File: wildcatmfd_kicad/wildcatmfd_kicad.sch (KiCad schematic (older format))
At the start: 21 parts, among them SW1 SW_Push, SW10 SW_Push, SW11 SW_Push, SW12 SW_Push, SW13 SW_Push, SW14 SW_Push, SW15 SW_Push, SW16 SW_Push, SW17 SW_Push, SW18 SW_Push, SW19 SW_Push, SW2 SW_Push, SW20 SW_Push, SW3 SW_Push, SW4 SW_Push, SW5 SW_Push, SW6 SW_Push, SW7 SW_Push, SW8 SW_Push, SW9 SW_Push, U1 Teensy3.6

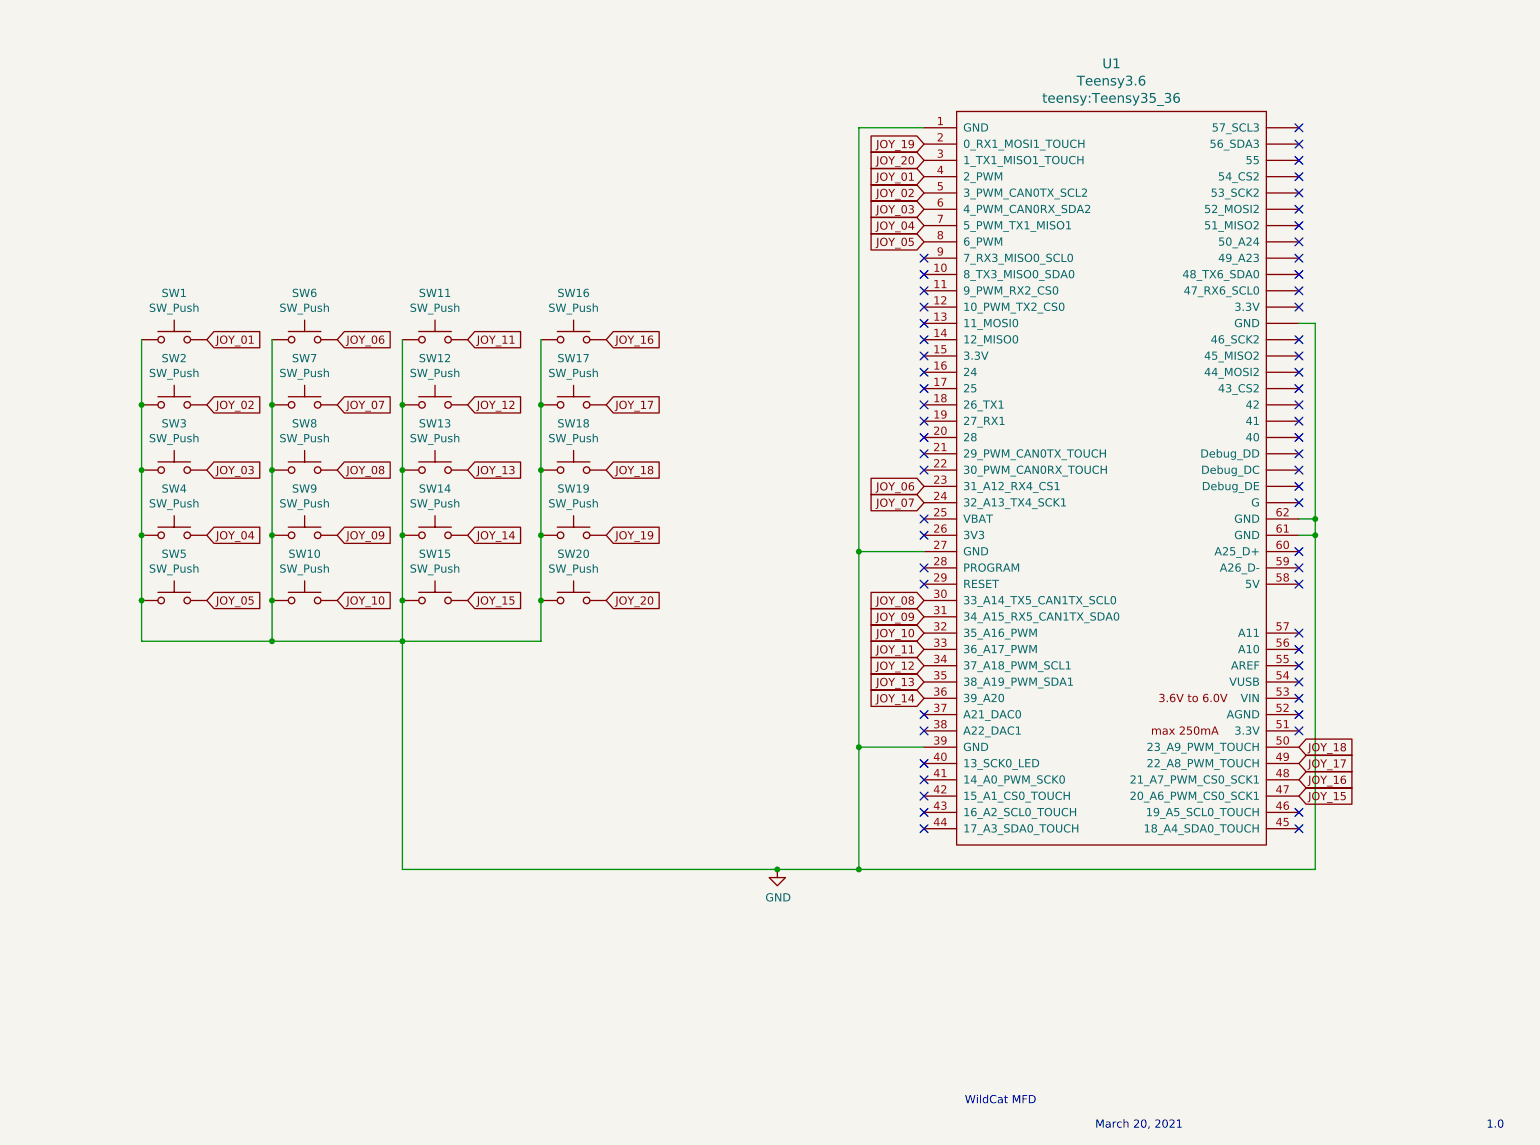
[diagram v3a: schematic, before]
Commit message: PCB 2.0
First attempt - 20mm off on screen mount (doh!) - Redesigning PCB to include pass-thru hole for HDMI ribbon cable and adding 3 pin header for +5v for screen power
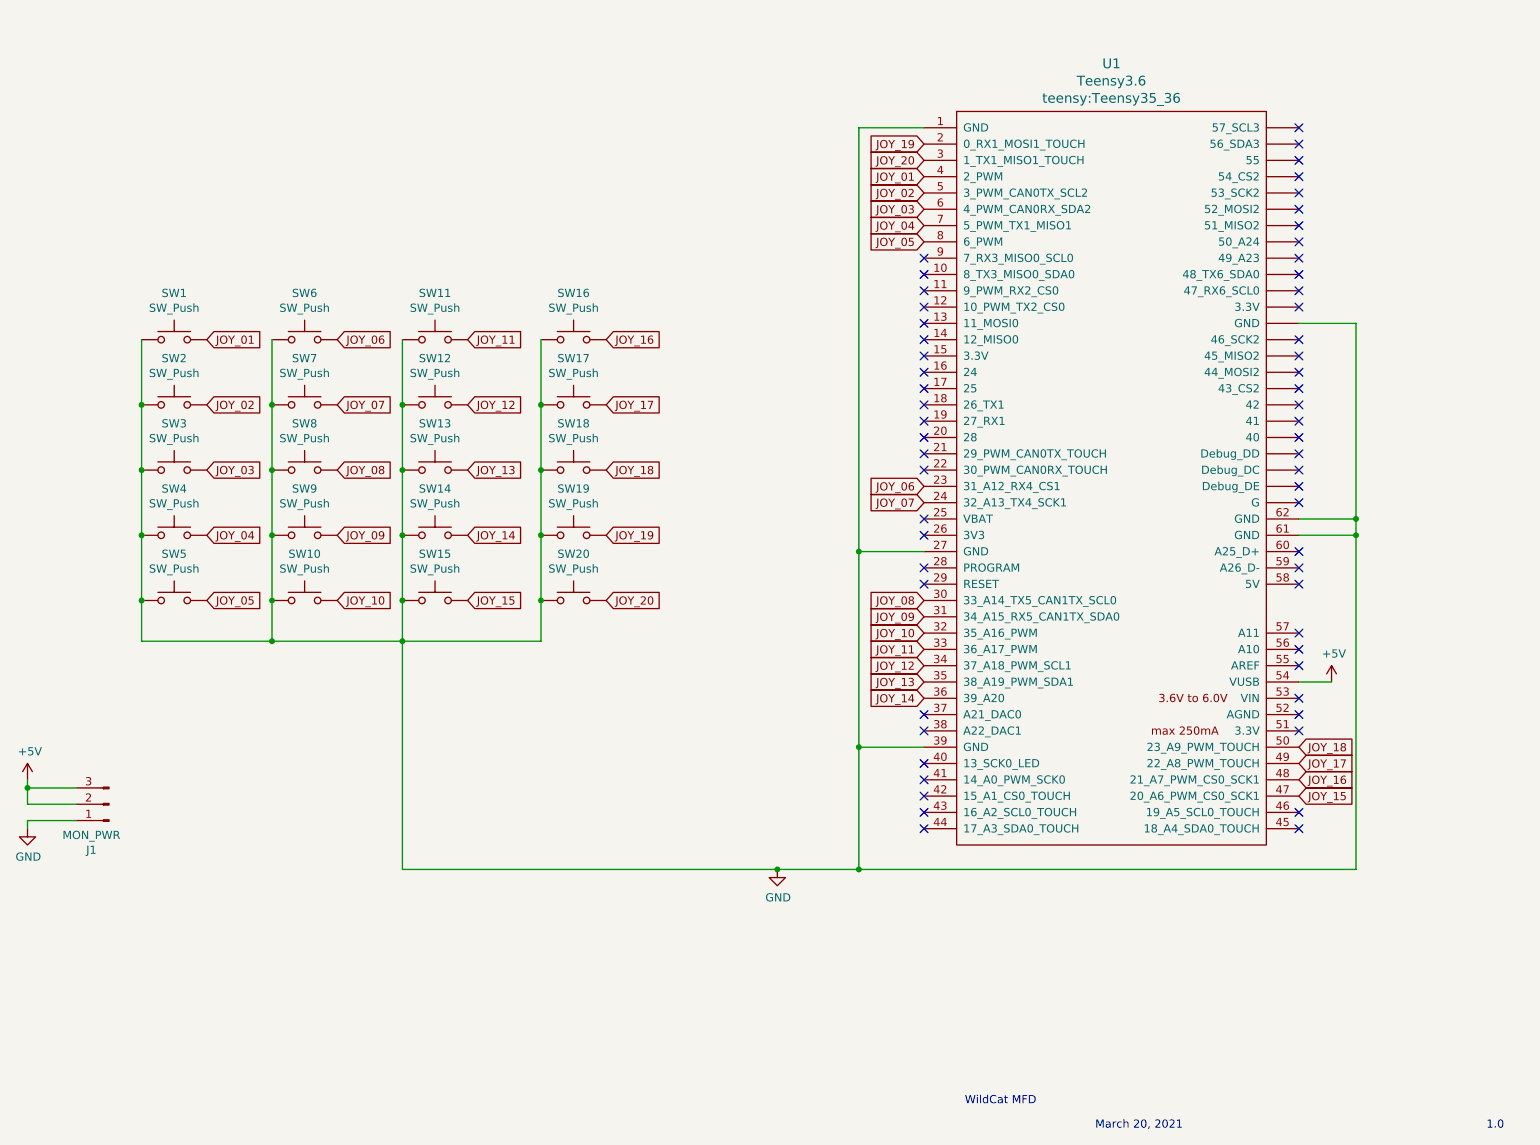
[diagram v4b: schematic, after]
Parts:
- added J1: MON_PWR, Connector_PinHeader_2.54mm:PinHeader_1x03_P2.54mm_Horizontal, symbol Connector:Conn_01x03_Male
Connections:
- net GND: now also J1.1 (Pin_1)
- net +5V: now reaches U1.54 (VUSB)
- net +5V: now also J1.2 (Pin_2), J1.3 (Pin_3)
- no-connect marks 60 -> 59
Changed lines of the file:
@@
 Comment4 ""
 $EndDescr
-$Comp
-L teensy:Teensy3.6 U1
-U 1 1 60563F5D
-P 8250 3650
-F 0 "U1" H 8250 6193 60  0000 C CNN
-F 1 "Teensy3.6" H 8250 6087 60  0000 C CNN
-F 2 "teensy:Teensy35_36" H 8250 5981 60  0000 C CNN
-F 3 "" H 8250 3700 60  0000 C CNN
-	1    8250 3650
-	1    0    0    -1
-$EndComp
 Text GLabel 7100 1800 0    50   Input ~ 0
 JOY_01
@@
 NoConn ~ 9400 4700
 NoConn ~ 9400 4800
-NoConn ~ 9400 4900
 NoConn ~ 9400 5000
 NoConn ~ 9400 5100
@@
 	6700 4100 6700 5300
 Wire Wire Line
-	9500 6050 9500 4000
-Wire Wire Line
-	9500 2700 9400 2700
-Wire Wire Line
-	9400 3900 9500 3900
-Connection ~ 9500 3900
-Wire Wire Line
-	9500 3900 9500 2700
-Wire Wire Line
-	9400 4000 9500 4000
-Connection ~ 9500 4000
-Wire Wire Line
-	9500 4000 9500 3900
+	9750 2700 9400 2700
 NoConn ~ 7100 2700
 Text GLabel 4300 4400 2    50   Input ~ 0
@@
 	3100 4650 3900 4650
 Wire Wire Line
-	6700 6050 9500 6050
+	6700 6050 9750 6050
 Wire Wire Line
 	6700 5300 7100 5300
@@
 NoConn ~ 7100 5700
 NoConn ~ 7100 5800
+Wire Wire Line
+	9750 3900 9750 2700
+Wire Wire Line
+	9400 3900 9750 3900
+Wire Wire Line
+	9400 4000 9750 4000
+Connection ~ 9750 3900
+Wire Wire Line
+	9750 4000 9750 3900
+Connection ~ 9750 4000
+Wire Wire Line
+	9750 6050 9750 4000
+$Comp
+L power:+5V #PWR04
+U 1 1 60764ECA
+P 9600 4900
+F 0 "#PWR04" H 9600 4750 50  0001 C CNN
+F 1 "+5V" H 9615 5073 50  0000 C CNN
+F 2 "" H 9600 4900 50  0001 C CNN
+F 3 "" H 9600 4900 50  0001 C CNN
+	1    9600 4900
+	1    0    0    -1
+$EndComp
+$Comp
+L teensy:Teensy3.6 U1
+U 1 1 60563F5D
+P 8250 3650
+F 0 "U1" H 8250 6193 60  0000 C CNN
+F 1 "Teensy3.6" H 8250 6087 60  0000 C CNN
+F 2 "teensy:Teensy35_36" H 8250 5981 60  0000 C CNN
+F 3 "" H 8250 3700 60  0000 C CNN
+	1    8250 3650
+	1    0    0    -1
+$EndComp
+Wire Wire Line
+	9400 4900 9600 4900
+$Comp
+L Connector:Conn_01x03_Male J1
+U 1 1 607679C7
+P 2100 5650
+F 0 "J1" H 2208 5931 50  0000 C CNN
+F 1 "MON_PWR" H 2208 5840 50  0000 C CNN
+F 2 "Connector_PinHeader_2.54mm:PinHeader_1x03_P2.54mm_Horizontal" H 2100 5650 50  0001 C CNN
+F 3 "~" H 2100 5650 50  0001 C CNN
+	1    2100 5650
+	-1   0    0    1
+$EndComp
+$Comp
+L power:+5V #PWR02
+U 1 1 6076A725
+P 1600 5500
+F 0 "#PWR02" H 1600 5350 50  0001 C CNN
+F 1 "+5V" H 1615 5673 50  0000 C CNN
+F 2 "" H 1600 5500 50  0001 C CNN
+F 3 "" H 1600 5500 50  0001 C CNN
+	1    1600 5500
+	1    0    0    -1
+$EndComp
+$Comp
+L power:GND #PWR03
+U 1 1 6076AFC6
+P 1600 5800
+F 0 "#PWR03" H 1600 5550 50  0001 C CNN
+F 1 "GND" H 1605 5627 50  0000 C CNN
+F 2 "" H 1600 5800 50  0001 C CNN
+F 3 "" H 1600 5800 50  0001 C CNN
+	1    1600 5800
+	1    0    0    -1
+$EndComp
+Wire Wire Line
+	1900 5550 1600 5550
+Wire Wire Line
+	1600 5550 1600 5500
+Wire Wire Line
+	1900 5650 1600 5650
+Wire Wire Line
+	1600 5650 1600 5550
+Connection ~ 1600 5550
+Wire Wire Line
+	1900 5750 1600 5750
+Wire Wire Line
+	1600 5750 1600 5800
 $EndSCHEMATC
